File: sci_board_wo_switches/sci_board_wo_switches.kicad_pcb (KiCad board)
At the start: 4 copper layers, 80 x 80 mm, 184 parts, among them J1 Conn_01x03_Pin Vertical, J2 10155435-00011LF, J3 10051922-2410EHLF, J4 10051922-2410EHLF, J5 10051922-2410EHLF, J6 PC104 Conn_02x20_Odd_Even, J7 Conn_01x04_Pin Vertical, J8 Conn_01x05_Pin Vertical, J9 Conn_01x04_Pin Vertical, SW1 EVP-AA602W, SW2 EVP-AA602W, U1 STM32L496VGTx, U10 74LVC2G07, U11 MR25H10, U12 MT29F4G01ABAFDWB-IT:F TR, U13 MT29F4G01ABAFDWB-IT:F TR, U14 TPS631000DRLR, U15 TPS631000DRLR, U16 MCP23008T-E/SS, U17 INA226AIDGSR, U18 TPS22968QDMGRQ1, U19 TPS22968QDMGRQ1, U2 TCAN3414, U3 TCAN3414, U4 TPS22968QDMGRQ1, U5 TPS22968QDMGRQ1, U6 TPS22968QDMGRQ1, U7 TCA9546APWR, U8 TXB0108PWR, U9 TXB0106PWR, X1 24MHz, X2 10MHz, X3 32.768KHZ

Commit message: VRef+ meeds to be connected to VDDA, should not be left floating
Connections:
- C10 pad 1: Net-(U1-VDDA) -> /PMIC/VDDA
- C14 pad 2: Net-(U1-VREF+) -> /PMIC/VDDA
- C15 pad 2: Net-(U1-VREF+) -> /PMIC/VDDA
- C9 pad 1: Net-(U1-VDDA) -> /PMIC/VDDA
- FB1 pad 2: Net-(U1-VDDA) -> /PMIC/VDDA
- U1 pad 21: Net-(U1-VREF+) -> /PMIC/VDDA
- U1 pad 22: Net-(U1-VDDA) -> /PMIC/VDDA
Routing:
- net /PMIC/VDDA: track 0.00 -> 8.45 mm
- net Net-(U1-VDDA): track 4.10 -> 0.00 mm
- net Net-(U1-VREF+): track 2.79 -> 0.00 mm
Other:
- board text added: "XXXX2025"
- board text removed: "06112025"

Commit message: SCI bodge board to correct I2C switching
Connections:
- U7 pad 11: GND -> /Cameras/Uniplexer/I2C_SDA_D
- U7 pad 12: GND -> /Cameras/Uniplexer/I2C_SCK_D
- U7 pad 14: /I2C1_SDA -> /I2C1_SCK
- U7 pad 15: /I2C1_SCK -> /I2C1_SDA
- U7 pad 4: /Cameras/Camera_A/SCK -> /Cameras/Camera_A/SDA
- U7 pad 5: /Cameras/Camera_A/SDA -> /Cameras/Camera_A/SCK
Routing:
- net /Cameras/Camera_A/SCK: track 19.2 -> 20.7 mm, vias 0 -> 2
- net /Cameras/Camera_A/SDA: track 20.3 -> 19.1 mm
- net /I2C1_SDA: track 61.2 -> 62.1 mm, vias 0 -> 2
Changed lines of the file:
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@@
 	(net 219 "unconnected-(RN11-R-Pad7)")
 	(net 220 "unconnected-(RN11-R-Pad8)")
+	(net 221 "/Cameras/Uniplexer/I2C_SDA_D")
+	(net 222 "/Cameras/Uniplexer/I2C_SCK_D")
 	(footprint "Capacitor_SMD:C_0805_2012Metric_Pad1.18x1.45mm_HandSolder"
 		(layer "F.Cu")
@@
 			(layers "F.Cu" "F.Mask" "F.Paste")
 			(roundrect_rratio 0.25)
-			(net 126 "/Cameras/Camera_A/SCK")
+			(net 117 "/Cameras/Camera_A/SDA")
 			(pinfunction "SD0")
 			(pintype "bidirectional")
@@
 			(layers "F.Cu" "F.Mask" "F.Paste")
 			(roundrect_rratio 0.25)
-			(net 117 "/Cameras/Camera_A/SDA")
+			(net 126 "/Cameras/Camera_A/SCK")
 			(pinfunction "SC0")
 			(pintype "bidirectional")
@@
 			(layers "F.Cu" "F.Mask" "F.Paste")
 			(roundrect_rratio 0.25)
-			(net 1 "GND")
+			(net 221 "/Cameras/Uniplexer/I2C_SDA_D")
 			(pinfunction "SD3")
-			(pintype "bidirectional")
+			(pintype "bidirectional+no_connect")
 		)
 		(pad "12" smd roundrect
@@
 			(layers "F.Cu" "F.Mask" "F.Paste")
 			(roundrect_rratio 0.25)
-			(net 1 "GND")
+			(net 222 "/Cameras/Uniplexer/I2C_SCK_D")
 			(pinfunction "SC3")
-			(pintype "bidirectional")
+			(pintype "bidirectional+no_connect")
 		)
 		(pad "13" smd roundrect
@@
 			(layers "F.Cu" "F.Mask" "F.Paste")
 			(roundrect_rratio 0.25)
-			(net 207 "/I2C1_SDA")
+			(net 206 "/I2C1_SCK")
 			(pinfunction "SCL")
 			(pintype "bidirectional")
@@
 			(layers "F.Cu" "F.Mask" "F.Paste")
 			(roundrect_rratio 0.25)
-			(net 206 "/I2C1_SCK")
+			(net 207 "/I2C1_SDA")
 			(pinfunction "SDA")
 			(pintype "bidirectional")
@@
 	)
 	(segment
-		(start 130.0585 114.884001)
-		(end 130.795999 114.884001)
+		(start 126.6 98.45)
+		(end 126.6 99.475)
 		(width 0.2)
 		(layer "F.Cu")
@@
 	)
 	(segment
-		(start 131.84 107.75)
-		(end 126.99 102.9)
+		(start 126.99 102.9)
+		(end 131.075 106.985)
 		(width 0.2)
 		(layer "F.Cu")
@@
 	)
 	(segment
-		(start 127.675 100.55)
-		(end 126.6 99.475)
+		(start 131.075 114)
+		(end 130.840999 114.234001)
 		(width 0.2)
 		(layer "F.Cu")
@@
 	)
 	(segment
-		(start 130.795999 114.884001)
-		(end 131.84 113.84)
+		(start 130.840999 114.234001)
+		(end 130.0585 114.234001)
 		(width 0.2)
 		(layer "F.Cu")
@@
 	(segment
 		(start 127.675 102.215)
-		(end 127.675 100.55)
+		(end 126.99 102.9)
 		(width 0.2)
 		(layer "F.Cu")
@@
 	)
 	(segment
-		(start 126.99 102.9)
+		(start 127.675 100.55)
 		(end 127.675 102.215)
 		(width 0.2)
@@
 	)
 	(segment
-		(start 131.84 113.84)
-		(end 131.84 107.75)
+		(start 126.6 99.475)
+		(end 127.675 100.55)
 		(width 0.2)
 		(layer "F.Cu")
@@
 	)
 	(segment
-		(start 126.6 99.475)
-		(end 126.6 98.45)
+		(start 131.075 106.985)
+		(end 131.075 114)
 		(width 0.2)
 		(layer "F.Cu")
@@
 	)
 	(segment
-		(start 131.481 113.549)
-		(end 131.481 108.081)
+		(start 130.740999 114.884001)
+		(end 130.0585 114.884001)
+		(width 0.2)
+		(layer "F.Cu")
+		(net 126)
+	)
+	(segment
+		(start 130.575 110.675)
+		(end 130.525 110.725)
+		(width 0.2)
+		(layer "F.Cu")
+		(net 126)
+	)
+	(segment
+		(start 131.641 113.984)
+		(end 130.740999 114.884001)
 		(width 0.2)
 		(layer "F.Cu")
@@
 	)
 	(segment
+		(start 125.9 102.5)
+		(end 125.9 99.2)
+		(width 0.2)
+		(layer "F.Cu")
+		(net 126)
+	)
+	(segment
 		(start 125.6 98.9)
 		(end 125.6 98.45)
@@
 	)
 	(segment
-		(start 131.481 108.081)
-		(end 125.9 102.5)
+		(start 131.641 110.725)
+		(end 131.641 113.916)
 		(width 0.2)
 		(layer "F.Cu")
@@
 	)
 	(segment
-		(start 130.795999 114.234001)
-		(end 131.481 113.549)
+		(start 130.575 107.175)
+		(end 125.9 102.5)
 		(width 0.2)
 		(layer "F.Cu")
@@
 	)
 	(segment
-		(start 125.9 102.5)
-		(end 125.9 99.2)
+		(start 130.575 107.175)
+		(end 130.575 110.675)
 		(width 0.2)
 		(layer "F.Cu")
@@
 	)
 	(segment
-		(start 130.0585 114.234001)
-		(end 130.795999 114.234001)
+		(start 131.641 113.916)
+		(end 131.641 113.984)
 		(width 0.2)
 		(layer "F.Cu")
 		(net 126)
 	)
+	(via
+		(at 130.525 110.725)
+		(size 0.6)
+		(drill 0.3)
+		(layers "F.Cu" "B.Cu")
+		(net 126)
+	)
+	(via
+		(at 131.641 110.725)
+		(size 0.6)
+		(drill 0.3)
+		(layers "F.Cu" "B.Cu")
+		(net 126)
+	)
+	(segment
+		(start 130.525 110.725)
+		(end 131.641 110.725)
+		(width 0.2)
+		(layer "B.Cu")
+		(net 126)
+	)
 	(segment
 		(start 118.6 82.4)
@@
 	)
 	(segment
-		(start 138.041 118.871)
-		(end 138.041 120.038232)
+		(start 138.041 120.038232)
+		(end 135.731232 122.348)
 		(width 0.2)
 		(layer "F.Cu")
@@
 	)
 	(segment
-		(start 135.8035 112.914001)
-		(end 136.656 112.914001)
+		(start 135.7835 113.584001)
+		(end 137.326 113.584001)
 		(width 0.2)
 		(layer "F.Cu")
@@
 	)
 	(segment
-		(start 103.132389 101.3)
-		(end 100.95 101.3)
-		(width 0.2)
-		(layer "F.Cu")
-		(net 206)
-	)
-	(segment
 		(start 108.676894 122.348)
 		(end 103.995591 117.666696)
@@
 	)
 	(segment
-		(start 137.59 113.848001)
-		(end 137.59 118.42)
+		(start 137.65 118.48)
+		(end 138.041 118.871)
 		(width 0.2)
 		(layer "F.Cu")
@@
 	)
 	(segment
-		(start 135.731232 122.348)
-		(end 108.676894 122.348)
+		(start 103.132389 101.3)
+		(end 100.95 101.3)
 		(width 0.2)
 		(layer "F.Cu")
@@
 	)
 	(segment
-		(start 137.59 118.42)
-		(end 138.041 118.871)
+		(start 138.041 118.871)
+		(end 138.041 120.038232)
 		(width 0.2)
 		(layer "F.Cu")
@@
 	)
 	(segment
-		(start 136.656 112.914001)
-		(end 137.59 113.848001)
+		(start 135.731232 122.348)
+		(end 108.676894 122.348)
 		(width 0.2)
 		(layer "F.Cu")
@@
 	)
 	(segment
-		(start 138.041 120.038232)
-		(end 135.731232 122.348)
+		(start 103.995591 102.163202)
+		(end 103.132389 101.3)
 		(width 0.2)
 		(layer "F.Cu")
@@
 	)
 	(segment
-		(start 103.995591 102.163202)
-		(end 103.132389 101.3)
+		(start 137.326 113.584001)
+		(end 137.65 113.908001)
 		(width 0.2)
 		(layer "F.Cu")
@@
 	)
 	(segment
-		(start 133.313 121.997)
-		(end 108.822283 121.997)
+		(start 137.65 113.908001)
+		(end 137.65 118.48)
 		(width 0.2)
 		(layer "F.Cu")
-		(net 207)
+		(net 206)
 	)
 	(segment
-		(start 136.89 113.768001)
-		(end 136.89 118.42)
+		(start 135.7835 112.934001)
+		(end 136.984001 112.934001)
 		(width 0.2)
 		(layer "F.Cu")
@@
 	)
 	(segment
-		(start 104.349 117.523716)
-		(end 104.349 101.881)
+		(start 137 118.31)
+		(end 133.313 121.997)
 		(width 0.2)
 		(layer "F.Cu")
@@
 	)
 	(segment
-		(start 136.89 118.42)
-		(end 133.313 121.997)
+		(start 133.313 121.997)
+		(end 108.822283 121.997)
 		(width 0.2)
 		(layer "F.Cu")
@@
 	)
 	(segment
-		(start 136.686 113.564001)
-		(end 136.89 113.768001)
+		(start 137 114.15)
+		(end 137 118.31)
 		(width 0.2)
 		(layer "F.Cu")
@@
 	)
 	(segment
-		(start 135.8035 113.564001)
-		(end 136.686 113.564001)
+		(start 104.349 117.523716)
+		(end 104.349 101.881)
+		(width 0.2)
+		(layer "F.Cu")
+		(net 207)
+	)
+	(segment
+		(start 136.984001 112.934001)
+		(end 137 112.95)
 		(width 0.2)
 		(layer "F.Cu")
 		(net 207)
 	)
+	(via
+		(at 137 114.15)
+		(size 0.6)
+		(drill 0.3)
+		(layers "F.Cu" "B.Cu")
+		(net 207)
+	)
+	(via
+		(at 137 112.95)
+		(size 0.6)
+		(drill 0.3)
+		(layers "F.Cu" "B.Cu")
+		(net 207)
+	)
+	(segment
+		(start 137 112.95)
+		(end 137 114.15)
+		(width 0.2)
+		(layer "B.Cu")
+		(net 207)
+	)

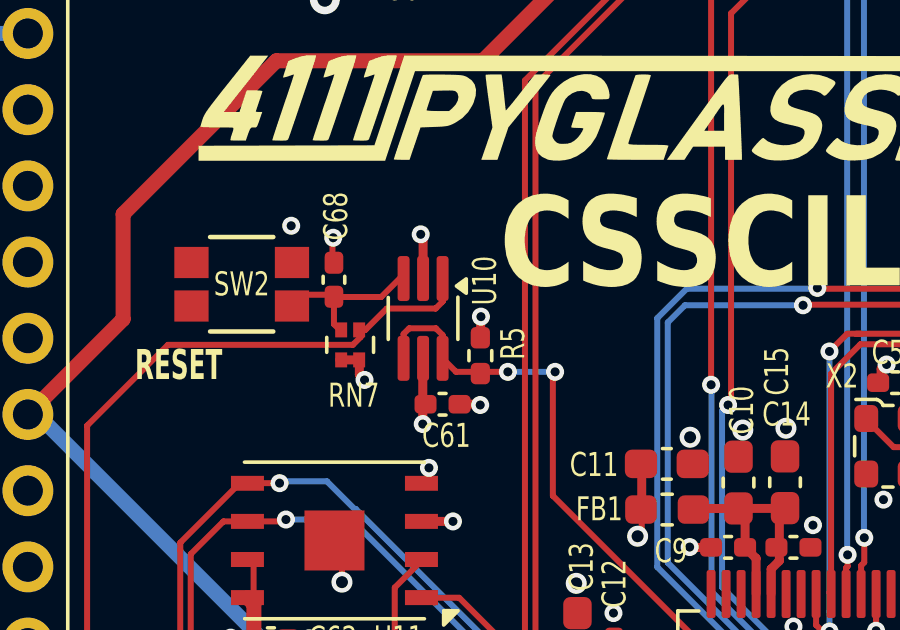
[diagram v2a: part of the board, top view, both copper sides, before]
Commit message: move commonly used hierarchical sheets to common/sheets for easy reuse
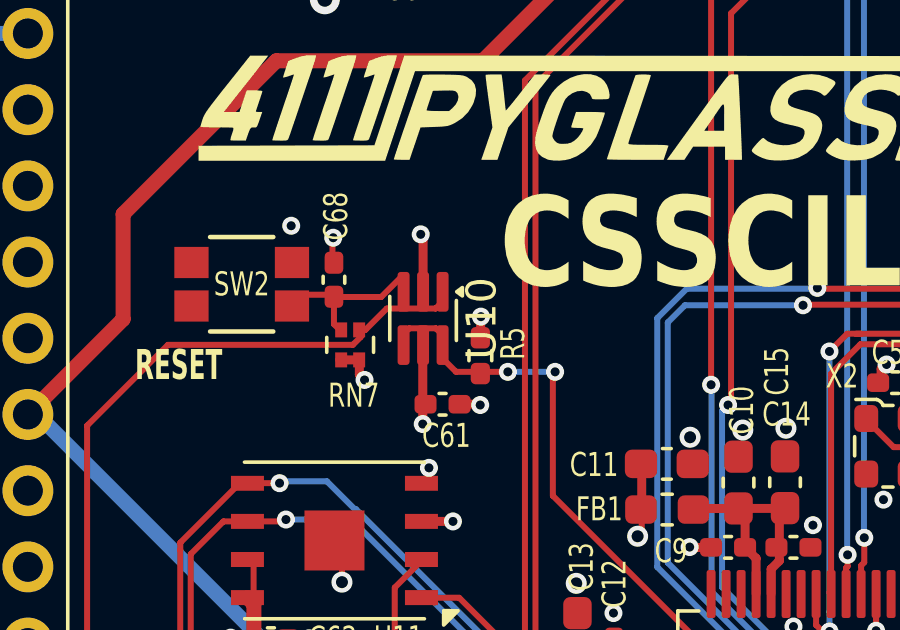
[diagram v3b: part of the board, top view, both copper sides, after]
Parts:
- U10: footprint Package_TO_SOT_SMD:SOT-363_SC-70-6_Handsoldering -> Package_TO_SOT_SMD:SOT-363_SC-70-6
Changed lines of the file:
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@@
 		(sheetname "/PMIC/DEBUG_INTERFACE/")
 		(sheetfile "../avionics_board/DEBUG_INTERFACE.kicad_sch")
-		(attr through_hole dnp)
+		(attr through_hole)
 		(fp_line
 			(start -1.38 -1.38)
@@
 		(sheetname "/PMIC/DEBUG_INTERFACE/")
 		(sheetfile "../avionics_board/DEBUG_INTERFACE.kicad_sch")
-		(attr through_hole dnp)
+		(attr through_hole)
 		(fp_line
 			(start -1.38 9)
@@
 		)
 	)
-	(footprint "Package_TO_SOT_SMD:SOT-363_SC-70-6_Handsoldering"
+	(footprint "Package_TO_SOT_SMD:SOT-363_SC-70-6"
 		(layer "F.Cu")
 		(at 77.674014 87.939628 -90)
-		(descr "SOT-363, SC-70-6, SC-88, Handsoldering")
-		(tags "SOT-363 SC-70-6 SC-88 Handsoldering")
+		(descr "SOT, 6 Pin (https://home.jeita.or.jp/tsc/std-pdf/ED-7500A.pdf#page=170, JEDEC MO-203, variant AB, https://www.jedec.org/document_search?search_api_views_fulltext=MO-203), generated with kicad-footprint-generator ipc_gullwing_generator.py")
+		(tags "SOT TO_SOT_SMD SC-88 SOT-363 SC-70-6 US6 UMT6 S-Mini6 TSSOP6")
 		(property "Reference" "U10"
-			(at -1.259628 -2.058986 90)
-			(unlocked yes)
+			(at 0 -1.95 270)
 			(layer "F.SilkS")
 			(effects
 				(font
-					(size 0.8 0.6)
+					(size 1 1)
 					(thickness 0.15)
 				)
@@
 		)
 		(property "Value" "74LVC2G07"
-			(at 0 2 90)
-			(unlocked yes)
+			(at 0 1.95 270)
 			(layer "F.Fab")
 			(effects
@@
 		(property "Datasheet" "https://www.ti.com/lit/ds/sces308l/sces308l.pdf"
 			(at 0 0 270)
-			(unlocked yes)
 			(layer "F.Fab")
 			(hide yes)
@@
 		(property "Description" "Noninverting buffer"
 			(at 0 0 270)
-			(unlocked yes)
 			(layer "F.Fab")
 			(hide yes)
@@
 		(attr smd)
 		(fp_line
-			(start -0.7 1.16)
-			(end 0.7 1.16)
+			(start 0.735 1.11)
+			(end -0.735 1.11)
 			(stroke
 				(width 0.12)
@@
 		)
 		(fp_line
-			(start -0.71 -1.16)
-			(end 0.7 -1.16)
+			(start -0.599252 -1.11)
+			(end 0.735 -1.11)
 			(stroke
 				(width 0.12)
@@
 		(fp_poly
 			(pts
-				(xy -1.08 -1.11) (xy -1.32 -1.44) (xy -0.84 -1.44) (xy -1.08 -1.11)
+				(xy -0.89 -1.12) (xy -1.03 -1.31) (xy -0.75 -1.31)
 			)
 			(stroke
@@
 		)
 		(fp_line
-			(start -2.4 1.4)
-			(end 2.4 1.4)
+			(start -0.88 1.25)
+			(end -0.88 1.1)
 			(stroke
 				(width 0.05)
@@
 		)
 		(fp_line
-			(start 2.4 1.4)
-			(end 2.4 -1.4)
+			(start 0.88 1.25)
+			(end -0.88 1.25)
 			(stroke
 				(width 0.05)
@@
 		)
 		(fp_line
-			(start -2.4 -1.4)
-			(end -2.4 1.4)
+			(start -1.8 1.1)
+			(end -1.8 -1.1)
 			(stroke
 				(width 0.05)
@@
 		)
 		(fp_line
-			(start -2.4 -1.4)
-			(end 2.4 -1.4)
+			(start -0.88 1.1)
+			(end -1.8 1.1)
 			(stroke
 				(width 0.05)
@@
 		)
 		(fp_line
-			(start 0.675 1.1)
-			(end -0.675 1.1)
+			(start 0.88 1.1)
+			(end 0.88 1.25)
 			(stroke
-				(width 0.1)
+				(width 0.05)
 				(type solid)
 			)
-			(layer "F.Fab")
+			(layer "F.CrtYd")
 		)
 		(fp_line
-			(start -0.675 -0.6)
-			(end -0.675 1.1)
+			(start 1.8 1.1)
+			(end 0.88 1.1)
 			(stroke
-				(width 0.1)
+				(width 0.05)
 				(type solid)
 			)
-			(layer "F.Fab")
+			(layer "F.CrtYd")
 		)
 		(fp_line
-			(start -0.175 -1.1)
-			(end -0.675 -0.6)
+			(start -1.8 -1.1)
+			(end -0.88 -1.1)
 			(stroke
-				(width 0.1)
+				(width 0.05)
 				(type solid)
 			)
-			(layer "F.Fab")
+			(layer "F.CrtYd")
 		)
 		(fp_line
-			(start 0.675 -1.1)
-			(end 0.675 1.1)
+			(start -0.88 -1.1)
+			(end -0.88 -1.25)
 			(stroke
-				(width 0.1)
+				(width 0.05)
 				(type solid)
 			)
-			(layer "F.Fab")
+			(layer "F.CrtYd")
+		)
+		(fp_line
+			(start 0.88 -1.1)
+			(end 1.8 -1.1)
+			(stroke
+				(width 0.05)
+				(type solid)
+			)
+			(layer "F.CrtYd")
+		)
+		(fp_line
+			(start 1.8 -1.1)
+			(end 1.8 1.1)
+			(stroke
+				(width 0.05)
+				(type solid)
+			)
+			(layer "F.CrtYd")
+		)
+		(fp_line
+			(start -0.88 -1.25)
+			(end 0.88 -1.25)
+			(stroke
+				(width 0.05)
+				(type solid)
+			)
+			(layer "F.CrtYd")
 		)
 		(fp_line
-			(start 0.675 -1.1)
-			(end -0.175 -1.1)
+			(start 0.88 -1.25)
+			(end 0.88 -1.1)
+			(stroke
+				(width 0.05)
+				(type solid)
+			)
+			(layer "F.CrtYd")
+		)
+		(fp_poly
+			(pts
+				(xy -0.3125 -1) (xy 0.625 -1) (xy 0.625 1) (xy -0.625 1) (xy -0.625 -0.6875)
+			)
 			(stroke
 				(width 0.1)
 				(type solid)
 			)
+			(fill no)
 			(layer "F.Fab")
 		)
 		(fp_text user "${REFERENCE}"
 			(at 0 0 0)
-			(unlocked yes)
 			(layer "F.Fab")
 			(effects
 				(font
-					(size 1 1)
-					(thickness 0.15)
+					(size 0.5 0.5)
+					(thickness 0.08)
 				)
 			)
 		)
 		(pad "1" smd roundrect
-			(at -1.33 -0.65 270)
-			(size 1.5 0.4)
+			(at -0.8875 -0.65 270)
+			(size 1.325 0.4)
 			(layers "F.Cu" "F.Mask" "F.Paste")
 			(roundrect_rratio 0.25)
@@
 		)
 		(pad "2" smd roundrect
-			(at -1.33 0 270)
-			(size 1.5 0.4)
+			(at -0.8875 0 270)
+			(size 1.325 0.4)
 			(layers "F.Cu" "F.Mask" "F.Paste")
 			(roundrect_rratio 0.25)
@@
 		)
 		(pad "3" smd roundrect
-			(at -1.33 0.65 270)
-			(size 1.5 0.4)
+			(at -0.8875 0.65 270)
+			(size 1.325 0.4)
 			(layers "F.Cu" "F.Mask" "F.Paste")
 			(roundrect_rratio 0.25)
@@
 		)
 		(pad "4" smd roundrect
-			(at 1.33 0.65 270)
-			(size 1.5 0.4)
+			(at 0.8875 0.65 270)
+			(size 1.325 0.4)
 			(layers "F.Cu" "F.Mask" "F.Paste")
 			(roundrect_rratio 0.25)
@@
 		)
 		(pad "5" smd roundrect
-			(at 1.33 0 270)
-			(size 1.5 0.4)
+			(at 0.8875 0 270)
+			(size 1.325 0.4)
 			(layers "F.Cu" "F.Mask" "F.Paste")
 			(roundrect_rratio 0.25)
@@
 		)
 		(pad "6" smd roundrect
-			(at 1.33 -0.65 270)
-			(size 1.5 0.4)
+			(at 0.8875 -0.65 270)
+			(size 1.325 0.4)
 			(layers "F.Cu" "F.Mask" "F.Paste")
 			(roundrect_rratio 0.25)
@@
 		)
 		(embedded_fonts no)
-		(model "${KICAD8_3DMODEL_DIR}/Package_TO_SOT_SMD.3dshapes/SOT-363_SC-70-6.wrl"
+		(model "${KICAD9_3DMODEL_DIR}/Package_TO_SOT_SMD.3dshapes/SOT-363_SC-70-6.step"
 			(offset
 				(xyz 0 0 0)

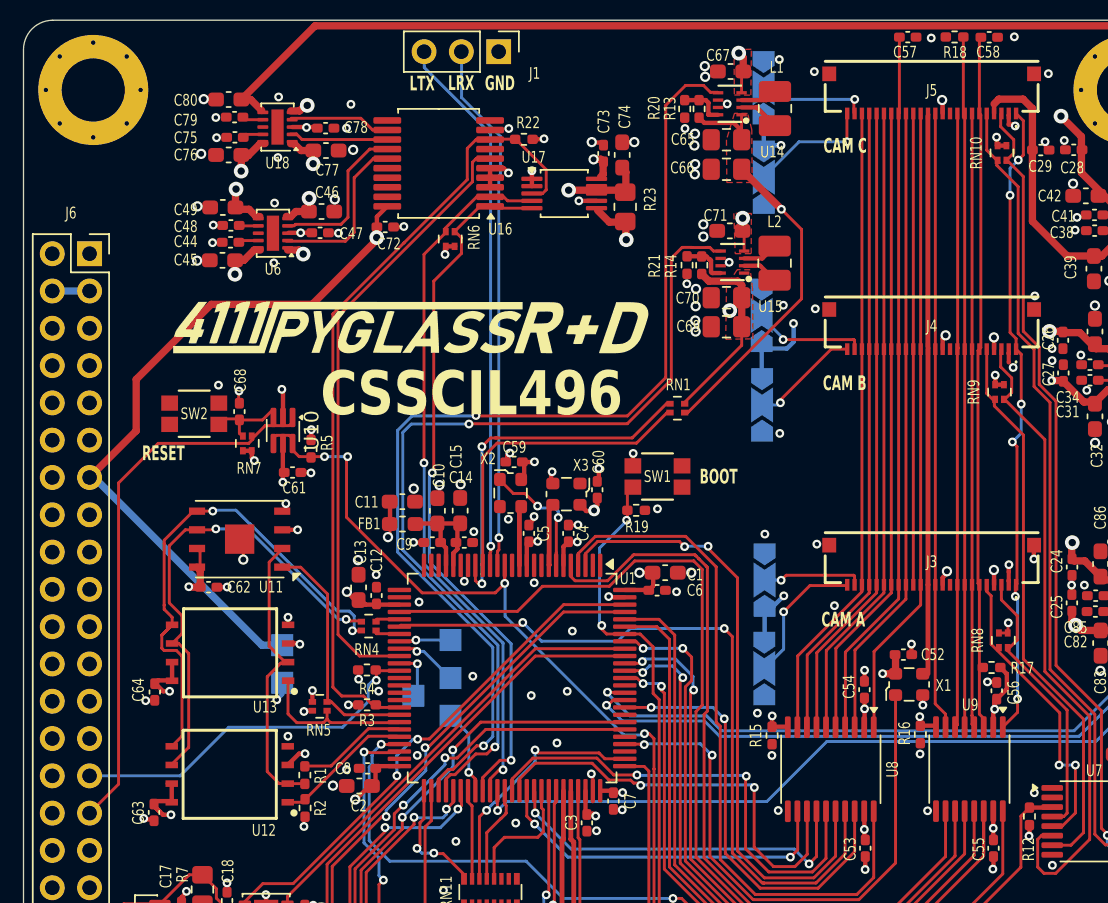
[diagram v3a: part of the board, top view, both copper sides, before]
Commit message: absolute paths for includes of includes or the second level common/sheet will cause problems!
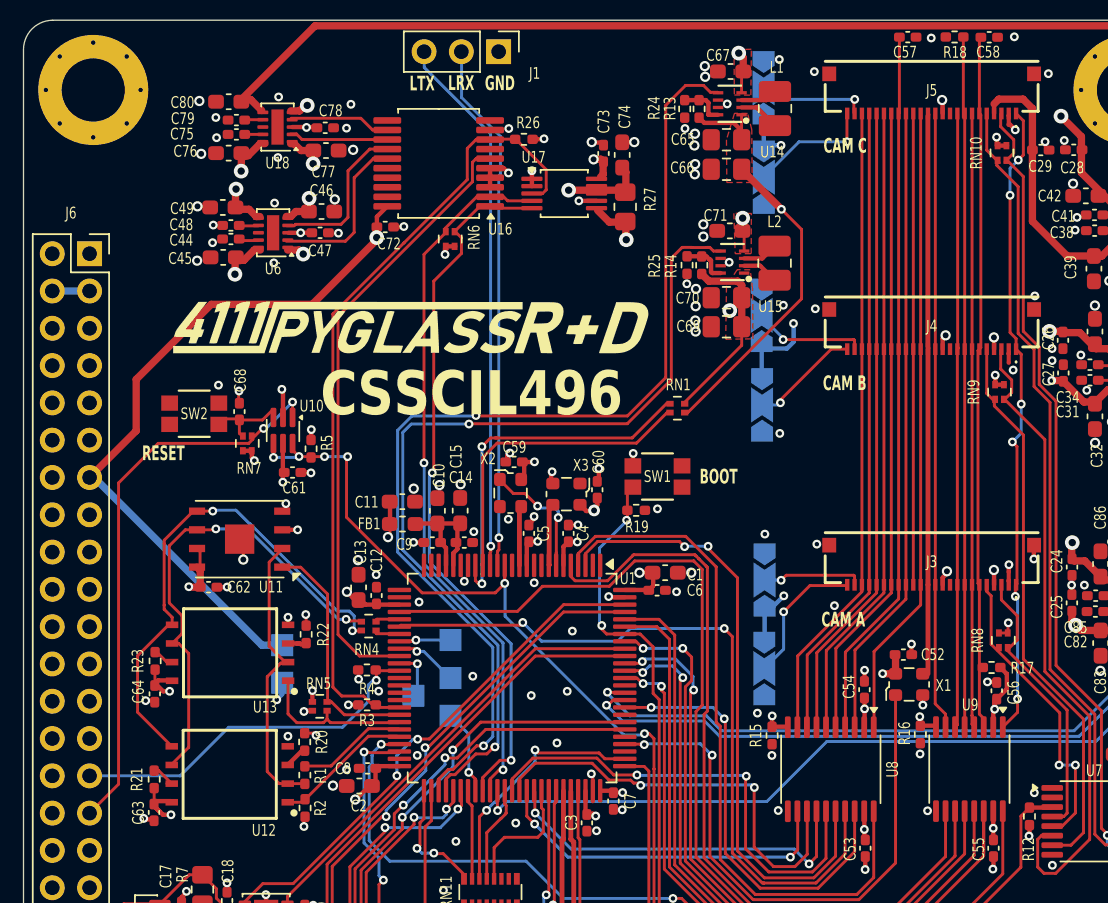
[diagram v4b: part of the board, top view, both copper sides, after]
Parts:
- added R20: 100K, Resistor_SMD:R_0402_1005Metric_Pad0.72x0.64mm_HandSolder, F.Cu at (79.2, 109.2)
- added R21: 100K, Resistor_SMD:R_0402_1005Metric_Pad0.72x0.64mm_HandSolder, F.Cu at (68.9, 111.7)
- added R22: 100K, Resistor_SMD:R_0402_1005Metric_Pad0.72x0.64mm_HandSolder, F.Cu at (79.2, 101.8)
- added R23: 100K, Resistor_SMD:R_0402_1005Metric_Pad0.72x0.64mm_HandSolder, F.Cu at (69.0, 103.6)
- moved C79 0.24 mm to (74.5, 66.8)
- moved C44 0.23 mm to (74.1, 74.9)
- moved C75 0.22 mm to (74.5, 67.8)
- moved C45 0.21 mm to (73.6, 76.2)
- moved C80 0.15 mm to (74.0, 65.5)
- moved C64 0.12 mm to (68.9, 105.9)
- moved C76 0.12 mm to (74.0, 69.0)
- renumbered R20 to R24, R21 to R25, R22 to R26, R23 to R27
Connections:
- U12 pad 3: /3V3_Flash -> Net-(U12-WP#/IO2)
- U12 pad 7: /3V3_Flash -> Net-(U12-HOLD#/IO3)
- U13 pad 3: /3V3_Flash -> Net-(U13-WP#/IO2)
- U13 pad 7: /3V3_Flash -> Net-(U13-HOLD#/IO3)
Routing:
- net Net-(U12-HOLD#/IO3): track 0.00 -> 1.90 mm
- net Net-(U12-WP#/IO2): track 0.00 -> 1.77 mm
- net /SCI_RESET: track 37.7 -> 39.3 mm, vias 0 -> 2
- net Net-(U13-HOLD#/IO3): track 0.00 -> 1.44 mm
- net /3V3_Flash: track 51.8 -> 50.4 mm
- net Net-(U13-WP#/IO2): track 0.00 -> 1.28 mm
- net /PMIC/NRST: track 86.3 -> 87.6 mm, vias 4 -> 6
- net /Flash1/SPI_MOSI: track 35.0 -> 34.5 mm
